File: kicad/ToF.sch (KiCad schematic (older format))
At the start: 7 parts, among them P1 ToF_Host, P2 ToF_Slave, U9 VL6180X

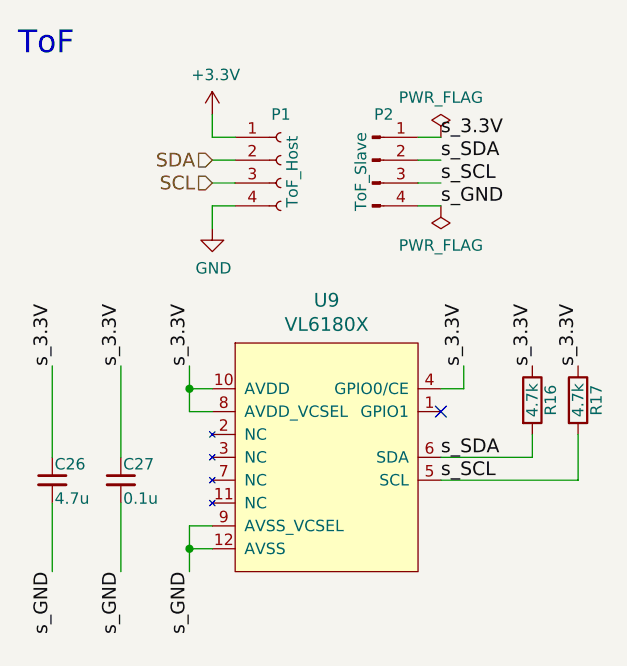
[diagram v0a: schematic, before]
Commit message: 部品を配置
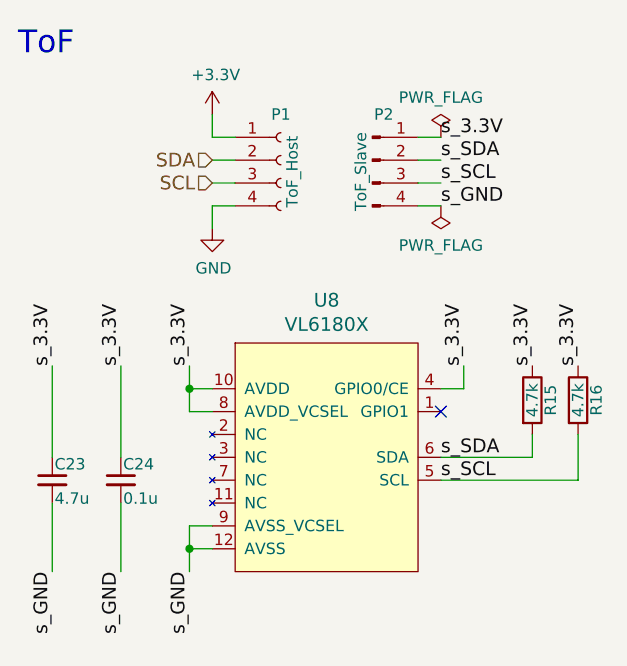
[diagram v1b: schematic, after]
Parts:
- renumbered C26 to C23, C27 to C24, R16 to R15, R17 to R16, U9 to U8
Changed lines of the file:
@@
 EESchema Schematic File Version 4
 LIBS:KERISE-cache
-EELAYER 26 0
+EELAYER 29 0
 EELAYER END
 $Descr A4 11693 8268
 encoding utf-8
-Sheet 15 15
+Sheet 15 13
 Title ""
 Date ""
@@
 SCL
 $Comp
-L Device:C_Small C27
+L Device:C_Small C24
 U 1 1 592BA26F
 P 3900 3800
-F 0 "C27" H 3910 3870 50  0000 L CNN
+F 0 "C24" H 3910 3870 50  0000 L CNN
 F 1 "0.1u" H 3910 3720 50  0000 L CNN
 F 2 "Capacitor_SMD:C_0201_0603Metric" H 3900 3800 50  0001 C CNN
@@
 $EndComp
 $Comp
-L Device:C_Small C26
+L Device:C_Small C23
 U 1 1 592BA2BF
 P 3600 3800
-F 0 "C26" H 3610 3870 50  0000 L CNN
+F 0 "C23" H 3610 3870 50  0000 L CNN
 F 1 "4.7u" H 3610 3720 50  0000 L CNN
 F 2 "Capacitor_SMD:C_0402_1005Metric" H 3600 3800 50  0001 C CNN
@@
 	5400 3400 5300 3400
 $Comp
-L Device:R R16
+L Device:R R15
 U 1 1 5AB6394F
 P 5700 3450
-F 0 "R16" V 5780 3450 50  0000 C CNN
+F 0 "R15" V 5780 3450 50  0000 C CNN
 F 1 "4.7k" V 5700 3450 50  0000 C CNN
 F 2 "Resistor_SMD:R_0201_0603Metric" V 5630 3450 50  0001 C CNN
@@
 $EndComp
 $Comp
-L Device:R R17
+L Device:R R16
 U 1 1 5AB639A9
 P 5900 3450
-F 0 "R17" V 5980 3450 50  0000 C CNN
+F 0 "R16" V 5980 3450 50  0000 C CNN
 F 1 "4.7k" V 5900 3450 50  0000 C CNN
 F 2 "Resistor_SMD:R_0201_0603Metric" V 5830 3450 50  0001 C CNN
@@
 	4200 3400 4200 3500
 $Comp
-L power:GND #PWR084
+L power:GND #PWR074
 U 1 1 5C29A844
 P 4300 2700
-F 0 "#PWR084" H 4300 2450 50  0001 C CNN
+F 0 "#PWR074" H 4300 2450 50  0001 C CNN
 F 1 "GND" H 4305 2527 50  0000 C CNN
 F 2 "" H 4300 2700 50  0001 C CNN
@@
 $EndComp
 $Comp
-L power:+3.3V #PWR083
+L power:+3.3V #PWR073
 U 1 1 5C29A8B4
 P 4300 2200
-F 0 "#PWR083" H 4300 2050 50  0001 C CNN
+F 0 "#PWR073" H 4300 2050 50  0001 C CNN
 F 1 "+3.3V" H 4315 2373 50  0000 C CNN
 F 2 "" H 4300 2200 50  0001 C CNN
@@
 $EndComp
 $Comp
-L KERISE:VL6180X U9
+L KERISE:VL6180X U8
 U 1 1 5C29B6B0
 P 4800 3300
-F 0 "U9" H 4800 3587 60  0000 C CNN
+F 0 "U8" H 4800 3587 60  0000 C CNN
 F 1 "VL6180X" H 4800 3481 60  0000 C CNN
 F 2 "mouse:VL6180X" H 4800 3300 60  0001 C CNN
